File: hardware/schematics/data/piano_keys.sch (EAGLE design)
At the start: 17 parts, among them X1 5566-2

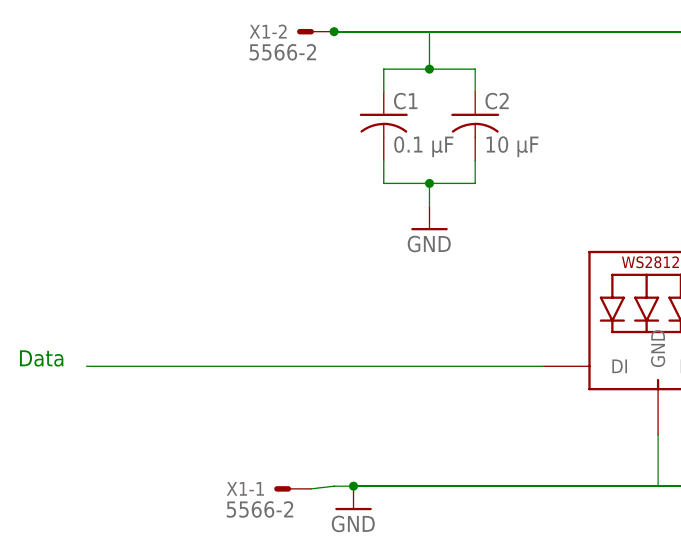
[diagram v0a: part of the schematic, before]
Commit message: adding the software component
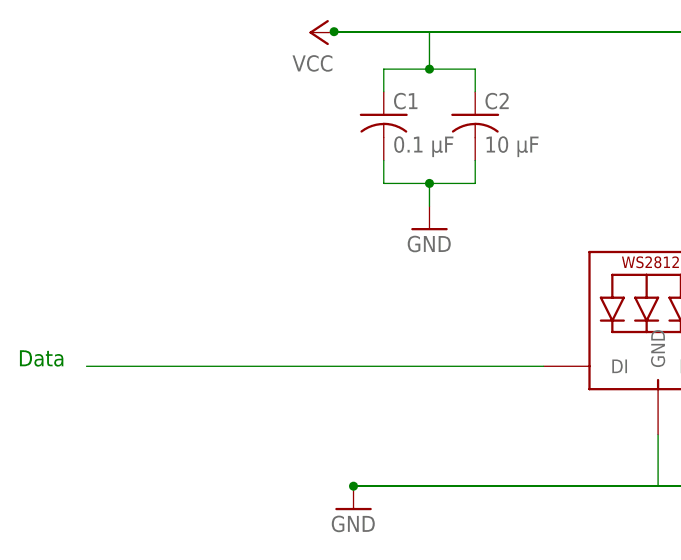
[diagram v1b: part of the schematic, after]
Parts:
- removed X1: 5566-2, con-molex:5566-2
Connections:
- net GND: no longer X1-1.S
- net N$13: no longer X1-2.S
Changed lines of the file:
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@@
 <?xml version="1.0" encoding="utf-8"?>
 <!DOCTYPE eagle SYSTEM "eagle.dtd">
-<eagle version="8.6.0">
+<eagle version="8.6.2">
 <drawing>
 <settings>
@@
 <layers>
 <layer number="1" name="Top" color="4" fill="1" visible="no" active="no"/>
+<layer number="2" name="Route2" color="1" fill="3" visible="no" active="no"/>
+<layer number="3" name="Route3" color="4" fill="3" visible="no" active="no"/>
+<layer number="4" name="Route4" color="1" fill="4" visible="no" active="no"/>
+<layer number="5" name="Route5" color="4" fill="4" visible="no" active="no"/>
+<layer number="6" name="Route6" color="1" fill="8" visible="no" active="no"/>
+<layer number="7" name="Route7" color="4" fill="8" visible="no" active="no"/>
+<layer number="8" name="Route8" color="1" fill="2" visible="no" active="no"/>
+<layer number="9" name="Route9" color="4" fill="2" visible="no" active="no"/>
+<layer number="10" name="Route10" color="1" fill="7" visible="no" active="no"/>
+<layer number="11" name="Route11" color="4" fill="7" visible="no" active="no"/>
+<layer number="12" name="Route12" color="1" fill="5" visible="no" active="no"/>
+<layer number="13" name="Route13" color="4" fill="5" visible="no" active="no"/>
+<layer number="14" name="Route14" color="1" fill="6" visible="no" active="no"/>
+<layer number="15" name="Route15" color="4" fill="6" visible="no" active="no"/>
 <layer number="16" name="Bottom" color="1" fill="1" visible="no" active="no"/>
 <layer number="17" name="Pads" color="2" fill="1" visible="no" active="no"/>
@@
 <part name="LED13" library="adafruit" deviceset="WS2812B" device="5050"/>
 <part name="LED14" library="adafruit" deviceset="WS2812B" device="5050"/>
-<part name="X1" library="con-molex" library_urn="urn:adsk.eagle:library:165" deviceset="5566-2" device=""/>
 <part name="C1" library="resistor" library_urn="urn:adsk.eagle:library:348" deviceset="C-US" device="025-024X044" package3d_urn="urn:adsk.eagle:package:26149/1" value="0.1 µF"/>
 <part name="C2" library="resistor" library_urn="urn:adsk.eagle:library:348" deviceset="C-US" device="025-024X044" package3d_urn="urn:adsk.eagle:package:26149/1" value="10 µF"/>
 <part name="GND2" library="supply1" library_urn="urn:adsk.eagle:library:371" deviceset="GND" device=""/>
+<part name="P+1" library="supply1" library_urn="urn:adsk.eagle:library:371" deviceset="VCC" device=""/>
 </parts>
 <sheets>
@@
 <instance part="LED13" gate="G$1" x="360" y="0"/>
 <instance part="LED14" gate="G$1" x="390" y="0"/>
-<instance part="X1" gate="-1" x="-41.08" y="-16.16" rot="R180"/>
-<instance part="X1" gate="-2" x="-38.54" y="34.64" rot="R180"/>
 <instance part="C1" gate="G$1" x="-30.48" y="25.4"/>
 <instance part="C2" gate="G$1" x="-20.32" y="25.4"/>
 <instance part="GND2" gate="1" x="-25.4" y="12.7"/>
+<instance part="P+1" gate="VCC" x="-38.608" y="34.544" rot="R90"/>
 </instances>
 <busses>
@@
 <wire x1="390" y1="-10.16" x2="390" y2="-15.86" width="0.1524" layer="91"/>
 <wire x1="390" y1="-15.86" x2="-33.84" y2="-15.86" width="0.1524" layer="91"/>
-<pinref part="X1" gate="-1" pin="S"/>
-<wire x1="-38.54" y1="-16.16" x2="-36" y2="-15.86" width="0.1524" layer="91"/>
-<wire x1="-36" y1="-15.86" x2="-33.84" y2="-15.86" width="0.1524" layer="91"/>
 </segment>
 <segment>
@@
 <wire x1="-25.4" y1="30.48" x2="-20.32" y2="30.48" width="0.1524" layer="91"/>
 <wire x1="-20.32" y1="30.48" x2="-20.32" y2="27.94" width="0.1524" layer="91"/>
-<pinref part="X1" gate="-2" pin="S"/>
 <pinref part="LED14" gate="G$1" pin="VDD"/>
 <wire x1="-36" y1="34.64" x2="395.08" y2="34.64" width="0.1524" layer="91"/>

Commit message: piano keys schematic and board
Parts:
- removed C1: 0.1 µF, resistor:C-US025-024X044
- removed C2: 10 µF, resistor:C-US025-024X044
- removed LED13, LED14: WS2812B5050, adafruit:WS2812B5050
- added SV1, SV2: (no value), con-lstb:MA04-1
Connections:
- removed net N$12 (its old number): LED12.DO, LED13.DI
- removed net N$13: C1.1, C2.1, LED1.VDD, LED10.VDD, LED11.VDD, LED12.VDD, LED14.VDD, LED2.VDD, LED3.VDD, LED4.VDD, LED5.VDD, LED6.VDD, LED7.VDD, LED8.VDD, LED9.VDD
- removed net N$14: LED13.VDD
- removed net N$15: LED1.DI
- new net 5V1: LED1.VDD, LED10.VDD, LED11.VDD, LED12.VDD, LED2.VDD, LED3.VDD, LED4.VDD, LED5.VDD, LED6.VDD, LED7.VDD, LED8.VDD, LED9.VDD, SV1.4, SV2.1
- new net DIN: LED1.DI, SV1.3
- new net DOUT: LED12.DO, SV1.2, SV2.3
- net GND: now also SV1.1, SV2.4; no longer C1.2, C2.2, LED13.GND, LED14.GND
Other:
- note removed: "Data"
